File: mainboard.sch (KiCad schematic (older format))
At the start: 32 parts, among them J101 To battery holder, J102 To RED display, J103 To GREEN display, J104 To BLUE display, Q101 Q_PNP_BCE, Q102 Q_NPN_BCE, SW101 STOP, SW102 START, SW103 GREEN, SW104 RED, SW105 BLUE, U101 LM555xN, U102 CD4015 for RED, U103 CD4015 for GREEN, U104 CD4015 for BLUE

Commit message: better layout
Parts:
- U1: renamed from U101; symbol Timer:LM555xN -> lm555:LM555_TIMER_PHY
- renumbered C101 to C1, D101 to D1, D102 to D2, J101 to J1, J102 to J2, J103 to J3, J104 to J4, Q101 to Q1, Q102 to Q2, R101 to R1, R110 to R10, R111 to R11, R112 to R12, R113 to R13, R106 to R2, R103 to R3, R102 to R4, R104 to R5, R105 to R6, R107 to R7, R108 to R8, R109 to R9, RV101 to RV1, SW103 to SW1, SW101 to SW2, SW102 to SW3, SW104 to SW4, SW105 to SW5, U102 to U2, U103 to U3, U104 to U4
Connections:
- net labels removed: discharge
- wire segments 162 -> 164
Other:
- moved on the sheet: C1, D2, R10, R11, R12, R13, R2, R3, R4, R8, R9, RV1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

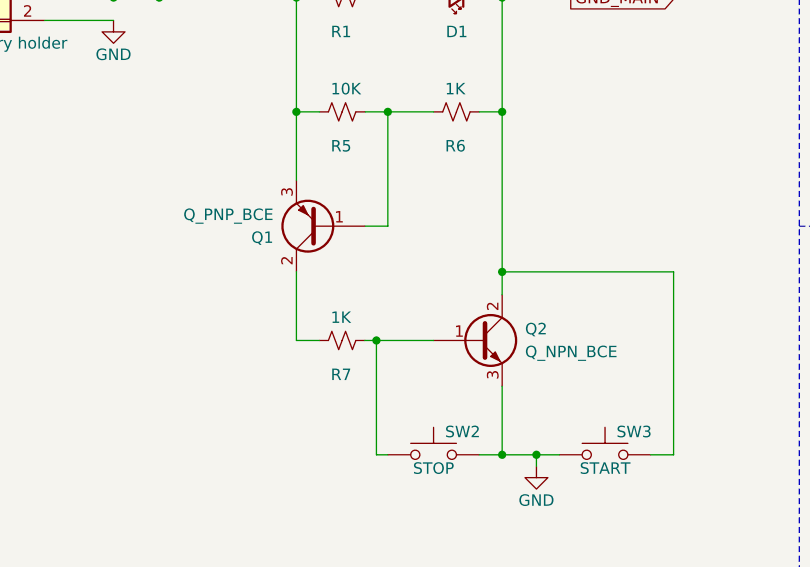
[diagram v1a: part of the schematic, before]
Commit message: noted actual parts for Q1, Q2 from the prototype
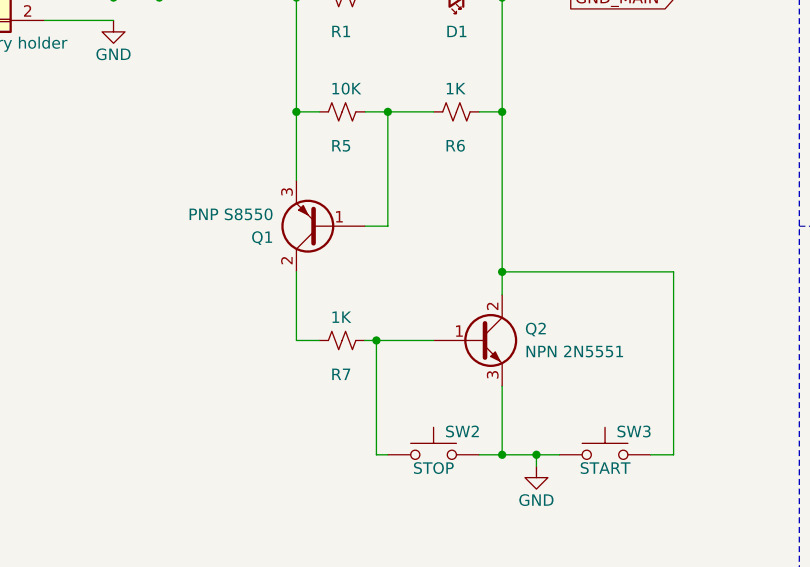
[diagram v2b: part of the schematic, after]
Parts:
- Q1: value Q_PNP_BCE -> PNP S8550
- Q2: value Q_NPN_BCE -> NPN 2N5551
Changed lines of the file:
@@
 P 2400 2500
 F 0 "Q1" H 2600 2550 50  0000 L CNN
-F 1 "Q_PNP_BCE" H 2600 2450 50  0000 L CNN
+F 1 "PNP S8550" H 2600 2450 50  0000 L CNN
 F 2 "" H 2600 2600 50  0001 C CNN
 F 3 "~" H 2400 2500 50  0001 C CNN
@@
 P 3100 3000
 F 0 "Q2" H 3300 3050 50  0000 L CNN
-F 1 "Q_NPN_BCE" H 3300 2950 50  0000 L CNN
+F 1 "NPN 2N5551" H 3300 2950 50  0000 L CNN
 F 2 "" H 3300 3100 50  0001 C CNN
 F 3 "~" H 3100 3000 50  0001 C CNN

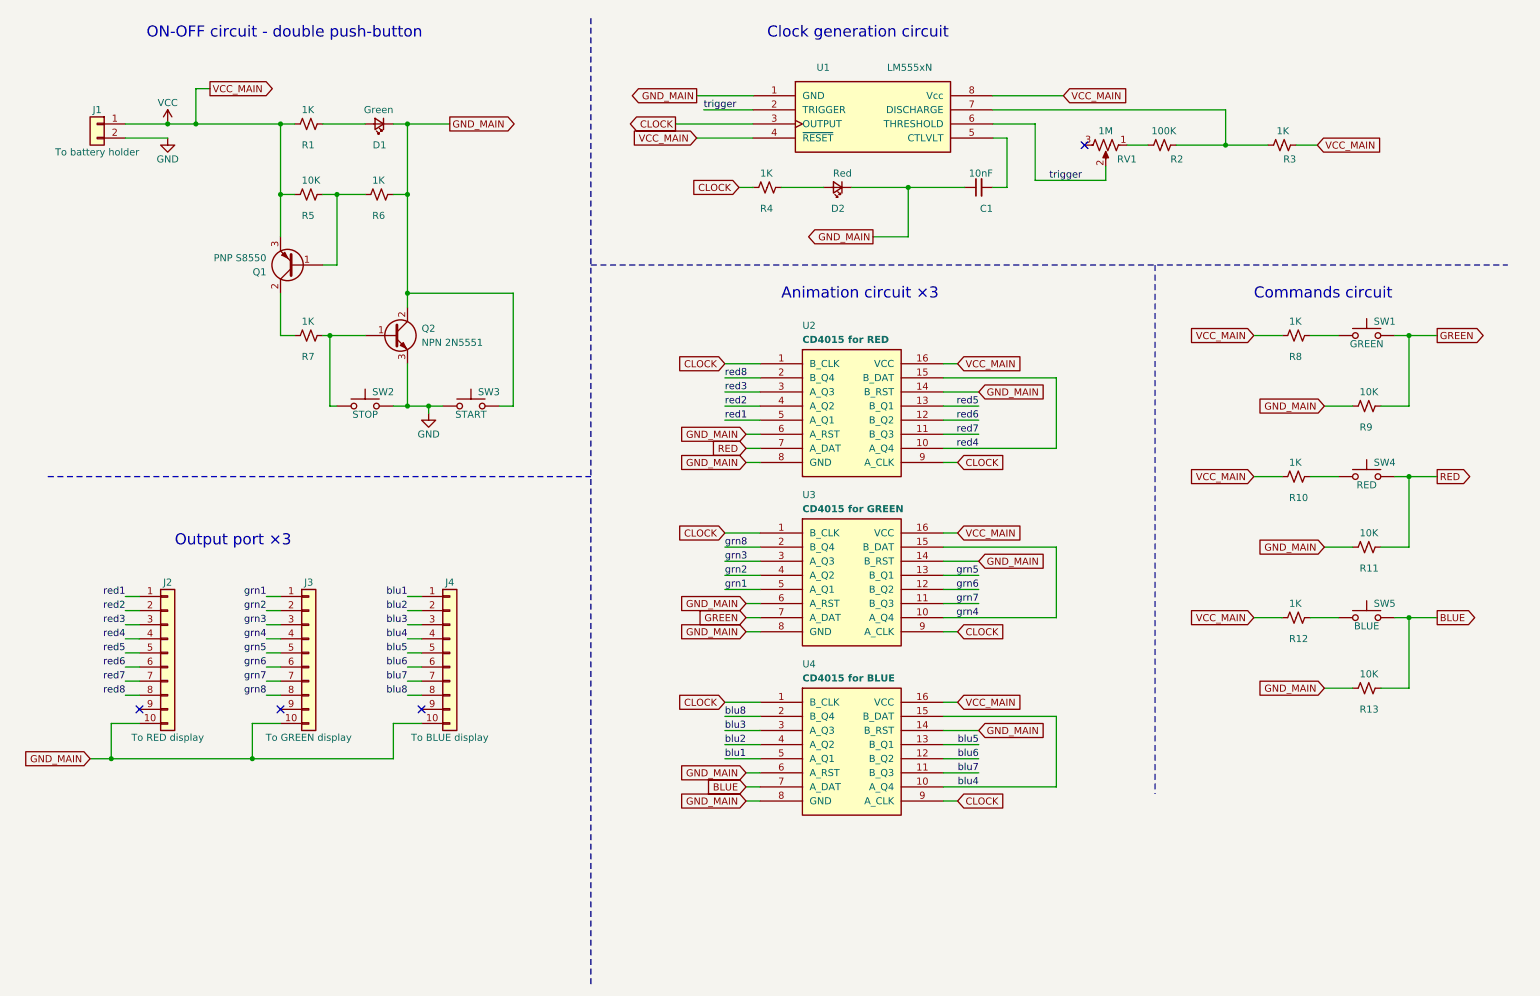
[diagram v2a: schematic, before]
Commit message: added bypass capacitors
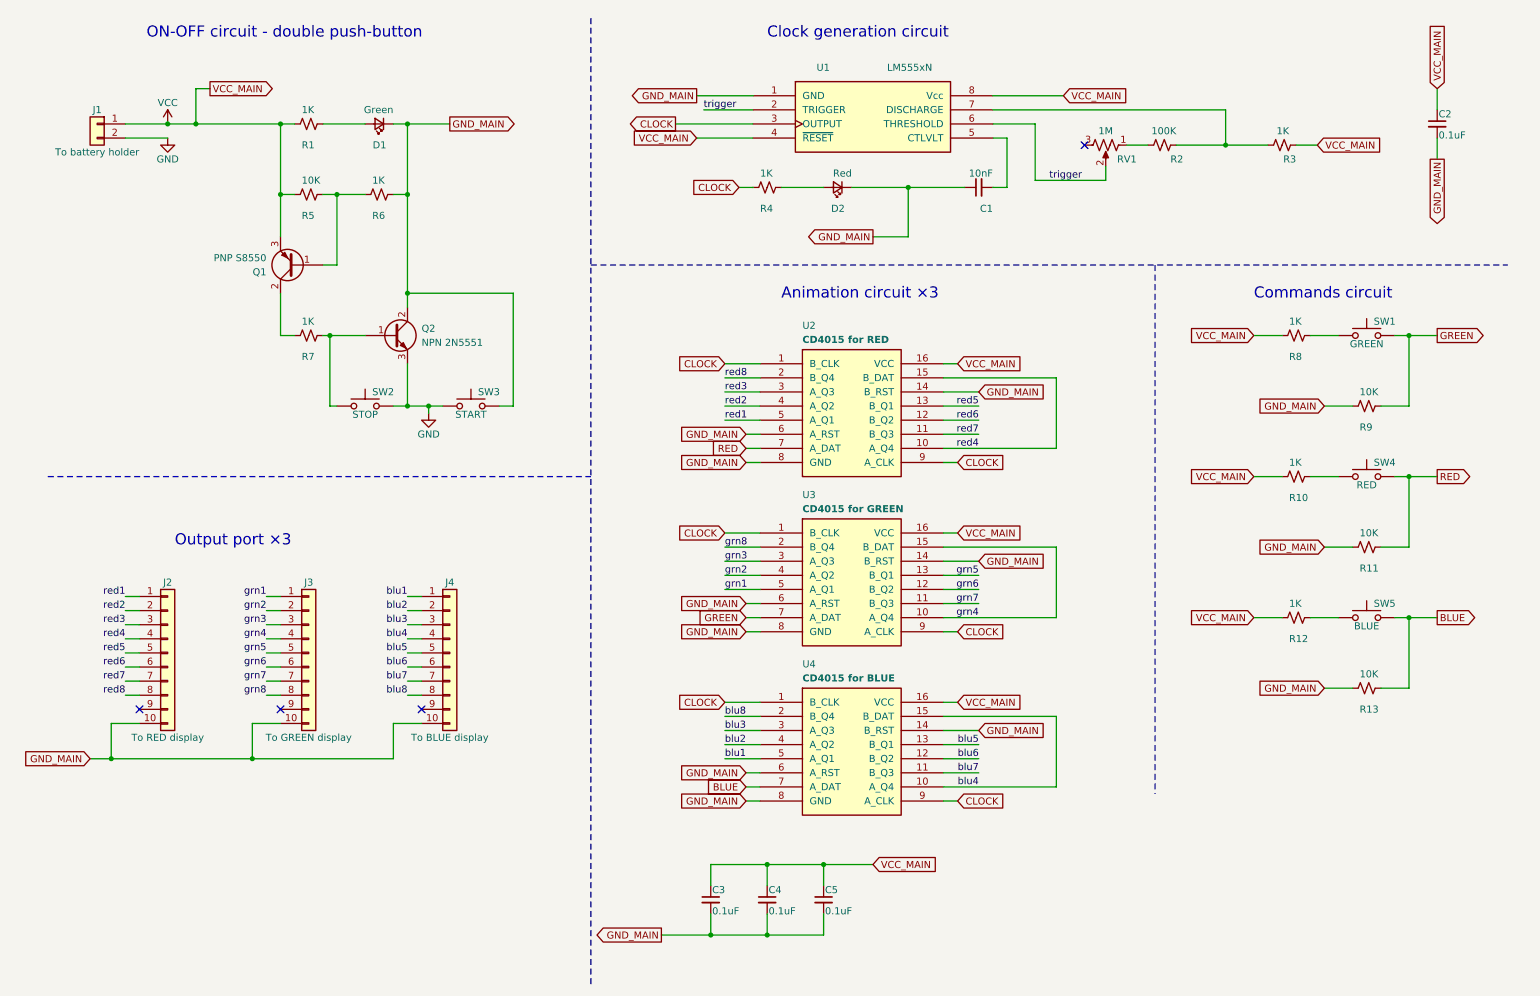
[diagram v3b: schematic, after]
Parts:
- added C2, C3, C4, C5: 0.1uF, symbol Device:C_Small
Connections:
- net GND_MAIN: now also C2.2, C3.2, C4.2, C5.2
- net VCC: now also C2.1, C3.1, C4.1, C5.1
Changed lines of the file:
@@
 Wire Notes Line
 	8500 2500 8500 6250
+$Comp
+L Device:C_Small C2
+U 1 1 6249338B
+P 10500 1500
+F 0 "C2" H 10510 1570 50  0000 L CNN
+F 1 "0.1uF" H 10510 1420 50  0000 L CNN
+F 2 "" H 10500 1500 50  0001 C CNN
+F 3 "~" H 10500 1500 50  0001 C CNN
+	1    10500 1500
+	1    0    0    -1
+$EndComp
+Text GLabel 10500 1250 1    50   Input ~ 0
+VCC_MAIN
+Text GLabel 10500 1750 3    50   Output ~ 0
+GND_MAIN
+Wire Wire Line
+	10500 1250 10500 1400
+Wire Wire Line
+	10500 1600 10500 1750
+$Comp
+L Device:C_Small C3
+U 1 1 624A9B0B
+P 5350 7000
+F 0 "C3" H 5360 7070 50  0000 L CNN
+F 1 "0.1uF" H 5360 6920 50  0000 L CNN
+F 2 "" H 5350 7000 50  0001 C CNN
+F 3 "~" H 5350 7000 50  0001 C CNN
+	1    5350 7000
+	1    0    0    -1
+$EndComp
+Text GLabel 6500 6750 2    50   Input ~ 0
+VCC_MAIN
+Text GLabel 5000 7250 0    50   Output ~ 0
+GND_MAIN
+Wire Wire Line
+	5350 6750 5350 6900
+Wire Wire Line
+	5350 7100 5350 7250
+$Comp
+L Device:C_Small C4
+U 1 1 624BF473
+P 5750 7000
+F 0 "C4" H 5760 7070 50  0000 L CNN
+F 1 "0.1uF" H 5760 6920 50  0000 L CNN
+F 2 "" H 5750 7000 50  0001 C CNN
+F 3 "~" H 5750 7000 50  0001 C CNN
+	1    5750 7000
+	1    0    0    -1
+$EndComp
+Wire Wire Line
+	5750 6750 5750 6900
+Wire Wire Line
+	5750 7100 5750 7250
+$Comp
+L Device:C_Small C5
+U 1 1 624CB4FE
+P 6150 7000
+F 0 "C5" H 6160 7070 50  0000 L CNN
+F 1 "0.1uF" H 6160 6920 50  0000 L CNN
+F 2 "" H 6150 7000 50  0001 C CNN
+F 3 "~" H 6150 7000 50  0001 C CNN
+	1    6150 7000
+	1    0    0    -1
+$EndComp
+Wire Wire Line
+	6150 6750 6150 6900
+Wire Wire Line
+	6150 7100 6150 7250
+Wire Wire Line
+	6500 6750 6150 6750
+Connection ~ 5750 6750
+Wire Wire Line
+	5750 6750 5350 6750
+Connection ~ 6150 6750
+Wire Wire Line
+	6150 6750 5750 6750
+Wire Wire Line
+	5000 7250 5350 7250
+Connection ~ 5350 7250
+Wire Wire Line
+	5350 7250 5750 7250
+Connection ~ 5750 7250
+Wire Wire Line
+	5750 7250 6150 7250
 $EndSCHEMATC

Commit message: assign footprints
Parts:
- C1, C2, C3, C4, C5: footprint (none) -> Capacitor_THT:C_Disc_D3.0mm_W1.6mm_P2.50mm
- D1, D2: footprint (none) -> LED_THT:LED_D3.0mm
- J1: footprint (none) -> Connector_PinHeader_2.54mm:PinHeader_1x02_P2.54mm_Horizontal
- J2, J3, J4: footprint (none) -> Connector_PinHeader_2.54mm:PinHeader_1x10_P2.54mm_Horizontal
- Q1, Q2: footprint (none) -> Package_TO_SOT_THT:TO-92
- R1, R10, R11, R12, R13, R2, R3, R4, R5, R6, R7, R8, R9: footprint (none) -> Resistor_THT:R_Axial_DIN0207_L6.3mm_D2.5mm_P10.16mm_Horizontal
- RV1: footprint (none) -> Potentiometer_THT:Potentiometer_Piher_PT-6-V_Vertical
- SW1, SW2, SW3, SW4, SW5: footprint (none) -> Button_Switch_THT:SW_PUSH-12mm
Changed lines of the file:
@@
 F 0 "J1" H 1000 1600 50  0000 C CNN
 F 1 "To battery holder" H 1000 1300 50  0000 C CNN
-F 2 "" H 1000 1500 50  0001 C CNN
+F 2 "Connector_PinHeader_2.54mm:PinHeader_1x02_P2.54mm_Horizontal" H 1000 1500 50  0001 C CNN
 F 3 "~" H 1000 1500 50  0001 C CNN
 	1    1000 1500
@@
 F 0 "R1" V 2650 1450 50  0000 L CNN
 F 1 "1K" V 2400 1450 50  0000 L CNN
-F 2 "" H 2500 1500 50  0001 C CNN
+F 2 "Resistor_THT:R_Axial_DIN0207_L6.3mm_D2.5mm_P10.16mm_Horizontal" H 2500 1500 50  0001 C CNN
 F 3 "~" H 2500 1500 50  0001 C CNN
 	1    2500 1500
@@
 F 0 "D1" H 2950 1650 50  0000 L CNN
 F 1 "Green" H 2900 1400 50  0000 L CNN
-F 2 "" V 3000 1500 50  0001 C CNN
+F 2 "LED_THT:LED_D3.0mm" V 3000 1500 50  0001 C CNN
 F 3 "~" V 3000 1500 50  0001 C CNN
 	1    3000 1500
@@
 F 0 "R5" V 2650 1950 50  0000 L CNN
 F 1 "10K" V 2400 1950 50  0000 L CNN
-F 2 "" H 2500 2000 50  0001 C CNN
+F 2 "Resistor_THT:R_Axial_DIN0207_L6.3mm_D2.5mm_P10.16mm_Horizontal" H 2500 2000 50  0001 C CNN
 F 3 "~" H 2500 2000 50  0001 C CNN
 	1    2500 2000
@@
 F 0 "R6" V 3150 1950 50  0000 L CNN
 F 1 "1K" V 2900 1950 50  0000 L CNN
-F 2 "" H 3000 2000 50  0001 C CNN
+F 2 "Resistor_THT:R_Axial_DIN0207_L6.3mm_D2.5mm_P10.16mm_Horizontal" H 3000 2000 50  0001 C CNN
 F 3 "~" H 3000 2000 50  0001 C CNN
 	1    3000 2000
@@
 F 0 "Q1" H 2600 2550 50  0000 L CNN
 F 1 "PNP S8550" H 2600 2450 50  0000 L CNN
-F 2 "" H 2600 2600 50  0001 C CNN
+F 2 "Package_TO_SOT_THT:TO-92" H 2600 2600 50  0001 C CNN
 F 3 "~" H 2400 2500 50  0001 C CNN
 	1    2400 2500
@@
 F 0 "R7" V 2650 2950 50  0000 L CNN
 F 1 "1K" V 2400 2950 50  0000 L CNN
-F 2 "" H 2500 3000 50  0001 C CNN
+F 2 "Resistor_THT:R_Axial_DIN0207_L6.3mm_D2.5mm_P10.16mm_Horizontal" H 2500 3000 50  0001 C CNN
 F 3 "~" H 2500 3000 50  0001 C CNN
 	1    2500 3000
@@
 F 0 "Q2" H 3300 3050 50  0000 L CNN
 F 1 "NPN 2N5551" H 3300 2950 50  0000 L CNN
-F 2 "" H 3300 3100 50  0001 C CNN
+F 2 "Package_TO_SOT_THT:TO-92" H 3300 3100 50  0001 C CNN
 F 3 "~" H 3100 3000 50  0001 C CNN
 	1    3100 3000
@@
 F 0 "SW2" H 2950 3600 50  0000 L CNN
 F 1 "STOP" H 2900 3440 50  0000 C CNN
-F 2 "" H 2900 3700 50  0001 C CNN
+F 2 "Button_Switch_THT:SW_PUSH-12mm" H 2900 3700 50  0001 C CNN
 F 3 "~" H 2900 3700 50  0001 C CNN
 	1    2900 3500
@@
 F 0 "SW3" H 3700 3600 50  0000 L CNN
 F 1 "START" H 3650 3440 50  0000 C CNN
-F 2 "" H 3650 3700 50  0001 C CNN
+F 2 "Button_Switch_THT:SW_PUSH-12mm" H 3650 3700 50  0001 C CNN
 F 3 "~" H 3650 3700 50  0001 C CNN
 	1    3650 3500
@@
 F 0 "RV1" V 8250 1800 50  0000 C CNN
 F 1 "1M" V 8050 1650 50  0000 C CNN
-F 2 "" H 8150 1650 50  0001 C CNN
+F 2 "Potentiometer_THT:Potentiometer_Piher_PT-6-V_Vertical" H 8150 1650 50  0001 C CNN
 F 3 "~" H 8150 1650 50  0001 C CNN
 	1    8150 1650
@@
 F 0 "R2" V 8450 1500 50  0000 L CNN
 F 1 "100K" V 8650 1550 50  0000 L CNN
-F 2 "" H 8550 1650 50  0001 C CNN
+F 2 "Resistor_THT:R_Axial_DIN0207_L6.3mm_D2.5mm_P10.16mm_Horizontal" H 8550 1650 50  0001 C CNN
 F 3 "~" H 8550 1650 50  0001 C CNN
 	1    8550 1650
@@
 F 0 "C1" V 7100 1850 50  0000 L CNN
 F 1 "10nF" V 7350 1850 50  0000 L CNN
-F 2 "" H 7250 1950 50  0001 C CNN
+F 2 "Capacitor_THT:C_Disc_D3.0mm_W1.6mm_P2.50mm" H 7250 1950 50  0001 C CNN
 F 3 "~" H 7250 1950 50  0001 C CNN
 	1    7250 1950
@@
 F 0 "R3" V 9300 1550 50  0000 L CNN
 F 1 "1K" V 9500 1600 50  0000 L CNN
-F 2 "" H 9400 1650 50  0001 C CNN
+F 2 "Resistor_THT:R_Axial_DIN0207_L6.3mm_D2.5mm_P10.16mm_Horizontal" H 9400 1650 50  0001 C CNN
 F 3 "~" H 9400 1650 50  0001 C CNN
 	1    9400 1650
@@
 F 0 "SW1" H 10050 3100 50  0000 L CNN
 F 1 "GREEN" H 10000 2940 50  0000 C CNN
-F 2 "" H 10000 3200 50  0001 C CNN
+F 2 "Button_Switch_THT:SW_PUSH-12mm" H 10000 3200 50  0001 C CNN
 F 3 "~" H 10000 3200 50  0001 C CNN
 	1    10000 3000
@@
 F 0 "SW4" H 10050 4100 50  0000 L CNN
 F 1 "RED" H 10000 3940 50  0000 C CNN
-F 2 "" H 10000 4200 50  0001 C CNN
+F 2 "Button_Switch_THT:SW_PUSH-12mm" H 10000 4200 50  0001 C CNN
 F 3 "~" H 10000 4200 50  0001 C CNN
 	1    10000 4000
@@
 F 0 "SW5" H 10050 5100 50  0000 L CNN
 F 1 "BLUE" H 10000 4940 50  0000 C CNN
-F 2 "" H 10000 5200 50  0001 C CNN
+F 2 "Button_Switch_THT:SW_PUSH-12mm" H 10000 5200 50  0001 C CNN
 F 3 "~" H 10000 5200 50  0001 C CNN
 	1    10000 5000
@@
 F 0 "R9" V 10150 3450 50  0000 L CNN
 F 1 "10K" V 9900 3450 50  0000 L CNN
-F 2 "" H 10000 3500 50  0001 C CNN
+F 2 "Resistor_THT:R_Axial_DIN0207_L6.3mm_D2.5mm_P10.16mm_Horizontal" H 10000 3500 50  0001 C CNN
 F 3 "~" H 10000 3500 50  0001 C CNN
 	1    10000 3500
@@
 F 0 "R8" V 9650 2950 50  0000 L CNN
 F 1 "1K" V 9400 2950 50  0000 L CNN
-F 2 "" H 9500 3000 50  0001 C CNN
+F 2 "Resistor_THT:R_Axial_DIN0207_L6.3mm_D2.5mm_P10.16mm_Horizontal" H 9500 3000 50  0001 C CNN
 F 3 "~" H 9500 3000 50  0001 C CNN
 	1    9500 3000
@@
 F 0 "R10" V 9650 3950 50  0000 L CNN
 F 1 "1K" V 9400 3950 50  0000 L CNN
-F 2 "" H 9500 4000 50  0001 C CNN
+F 2 "Resistor_THT:R_Axial_DIN0207_L6.3mm_D2.5mm_P10.16mm_Horizontal" H 9500 4000 50  0001 C CNN
 F 3 "~" H 9500 4000 50  0001 C CNN
 	1    9500 4000
@@
 F 0 "R12" V 9650 4950 50  0000 L CNN
 F 1 "1K" V 9400 4950 50  0000 L CNN
-F 2 "" H 9500 5000 50  0001 C CNN
+F 2 "Resistor_THT:R_Axial_DIN0207_L6.3mm_D2.5mm_P10.16mm_Horizontal" H 9500 5000 50  0001 C CNN
 F 3 "~" H 9500 5000 50  0001 C CNN
 	1    9500 5000
@@
 F 0 "R11" V 10150 4450 50  0000 L CNN
 F 1 "10K" V 9900 4450 50  0000 L CNN
-F 2 "" H 10000 4500 50  0001 C CNN
+F 2 "Resistor_THT:R_Axial_DIN0207_L6.3mm_D2.5mm_P10.16mm_Horizontal" H 10000 4500 50  0001 C CNN
 F 3 "~" H 10000 4500 50  0001 C CNN
 	1    10000 4500
@@
 F 0 "R13" V 10150 5450 50  0000 L CNN
 F 1 "10K" V 9900 5450 50  0000 L CNN
-F 2 "" H 10000 5500 50  0001 C CNN
+F 2 "Resistor_THT:R_Axial_DIN0207_L6.3mm_D2.5mm_P10.16mm_Horizontal" H 10000 5500 50  0001 C CNN
 F 3 "~" H 10000 5500 50  0001 C CNN
 	1    10000 5500
@@
 F 0 "R4" V 5900 1900 50  0000 L CNN
 F 1 "1K" V 5650 1900 50  0000 L CNN
-F 2 "" H 5750 1950 50  0001 C CNN
+F 2 "Resistor_THT:R_Axial_DIN0207_L6.3mm_D2.5mm_P10.16mm_Horizontal" H 5750 1950 50  0001 C CNN
 F 3 "~" H 5750 1950 50  0001 C CNN
 	1    5750 1950
@@
 F 0 "D2" H 6200 2100 50  0000 L CNN
 F 1 "Red" H 6150 1850 50  0000 L CNN
-F 2 "" V 6250 1950 50  0001 C CNN
+F 2 "LED_THT:LED_D3.0mm" V 6250 1950 50  0001 C CNN
 F 3 "~" V 6250 1950 50  0001 C CNN
 	1    6250 1950
@@
 F 0 "J2" H 1500 5750 50  0000 C CNN
 F 1 "To RED display" H 1500 4650 50  0000 C CNN
-F 2 "" H 1500 5250 50  0001 C CNN
+F 2 "Connector_PinHeader_2.54mm:PinHeader_1x10_P2.54mm_Horizontal" H 1500 5250 50  0001 C CNN
 F 3 "~" H 1500 5250 50  0001 C CNN
 	1    1500 5250
@@
 F 0 "J3" H 2500 5750 50  0000 C CNN
 F 1 "To GREEN display" H 2500 4650 50  0000 C CNN
-F 2 "" H 2500 5250 50  0001 C CNN
+F 2 "Connector_PinHeader_2.54mm:PinHeader_1x10_P2.54mm_Horizontal" H 2500 5250 50  0001 C CNN
 F 3 "~" H 2500 5250 50  0001 C CNN
 	1    2500 5250
@@
 F 0 "J4" H 3500 5750 50  0000 C CNN
 F 1 "To BLUE display" H 3500 4650 50  0000 C CNN
-F 2 "" H 3500 5250 50  0001 C CNN
+F 2 "Connector_PinHeader_2.54mm:PinHeader_1x10_P2.54mm_Horizontal" H 3500 5250 50  0001 C CNN
 F 3 "~" H 3500 5250 50  0001 C CNN
 	1    3500 5250
@@
 F 0 "C2" H 10510 1570 50  0000 L CNN
 F 1 "0.1uF" H 10510 1420 50  0000 L CNN
-F 2 "" H 10500 1500 50  0001 C CNN
+F 2 "Capacitor_THT:C_Disc_D3.0mm_W1.6mm_P2.50mm" H 10500 1500 50  0001 C CNN
 F 3 "~" H 10500 1500 50  0001 C CNN
 	1    10500 1500
@@
 F 0 "C3" H 5360 7070 50  0000 L CNN
 F 1 "0.1uF" H 5360 6920 50  0000 L CNN
-F 2 "" H 5350 7000 50  0001 C CNN
+F 2 "Capacitor_THT:C_Disc_D3.0mm_W1.6mm_P2.50mm" H 5350 7000 50  0001 C CNN
 F 3 "~" H 5350 7000 50  0001 C CNN
 	1    5350 7000
@@
 F 0 "C4" H 5760 7070 50  0000 L CNN
 F 1 "0.1uF" H 5760 6920 50  0000 L CNN
-F 2 "" H 5750 7000 50  0001 C CNN
+F 2 "Capacitor_THT:C_Disc_D3.0mm_W1.6mm_P2.50mm" H 5750 7000 50  0001 C CNN
 F 3 "~" H 5750 7000 50  0001 C CNN
 	1    5750 7000
@@
 F 0 "C5" H 6160 7070 50  0000 L CNN
 F 1 "0.1uF" H 6160 6920 50  0000 L CNN
-F 2 "" H 6150 7000 50  0001 C CNN
+F 2 "Capacitor_THT:C_Disc_D3.0mm_W1.6mm_P2.50mm" H 6150 7000 50  0001 C CNN
 F 3 "~" H 6150 7000 50  0001 C CNN
 	1    6150 7000

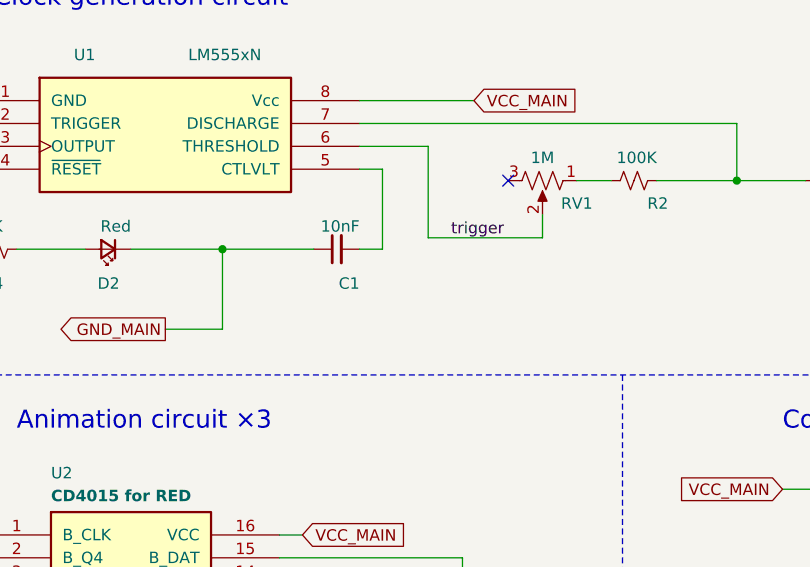
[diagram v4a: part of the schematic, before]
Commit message: added forgotten 1uF capacitor
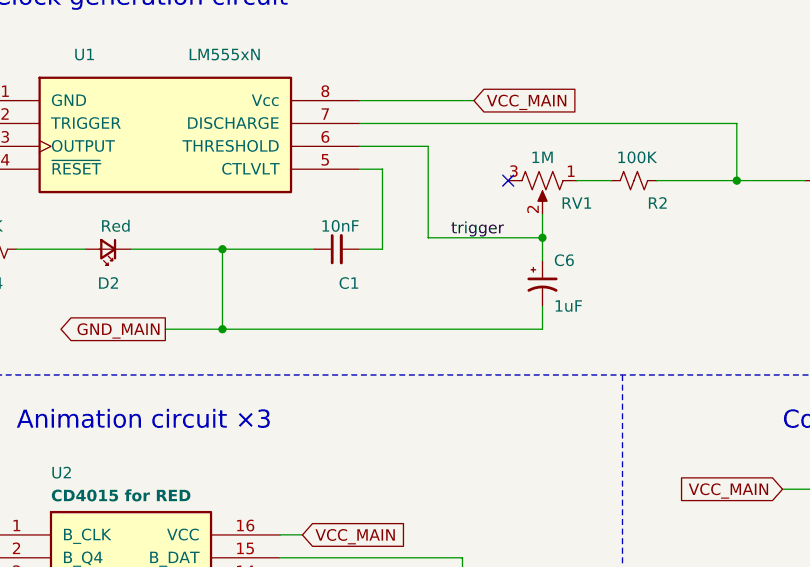
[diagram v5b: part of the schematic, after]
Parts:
- added C6: 1uF, Capacitor_THT:CP_Radial_D4.0mm_P1.50mm, symbol Device:CP1_Small
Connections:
- net GND_MAIN: now also C6.2
- net trigger: now also C6.1
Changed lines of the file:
@@
 Wire Wire Line
 	5750 7250 6150 7250
+$Comp
+L Device:CP1_Small C6
+U 1 1 6251FAFE
+P 8150 2100
+F 0 "C6" H 8200 2200 50  0000 L CNN
+F 1 "1uF" H 8200 2000 50  0000 L CNN
+F 2 "Capacitor_THT:CP_Radial_D4.0mm_P1.50mm" H 8150 2100 50  0001 C CNN
+F 3 "~" H 8150 2100 50  0001 C CNN
+	1    8150 2100
+	1    0    0    -1
+$EndComp
+Wire Wire Line
+	8150 2000 8150 1900
+Connection ~ 8150 1900
+Wire Wire Line
+	8150 2200 8150 2300
+Wire Wire Line
+	8150 2300 6750 2300
+Connection ~ 6750 2300
 $EndSCHEMATC
